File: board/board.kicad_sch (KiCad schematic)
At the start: 5 parts, among them J1 001_I2C, J2 001_I2C

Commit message: added LCSC part numbers
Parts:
- C3: lcsc (none) -> C15849

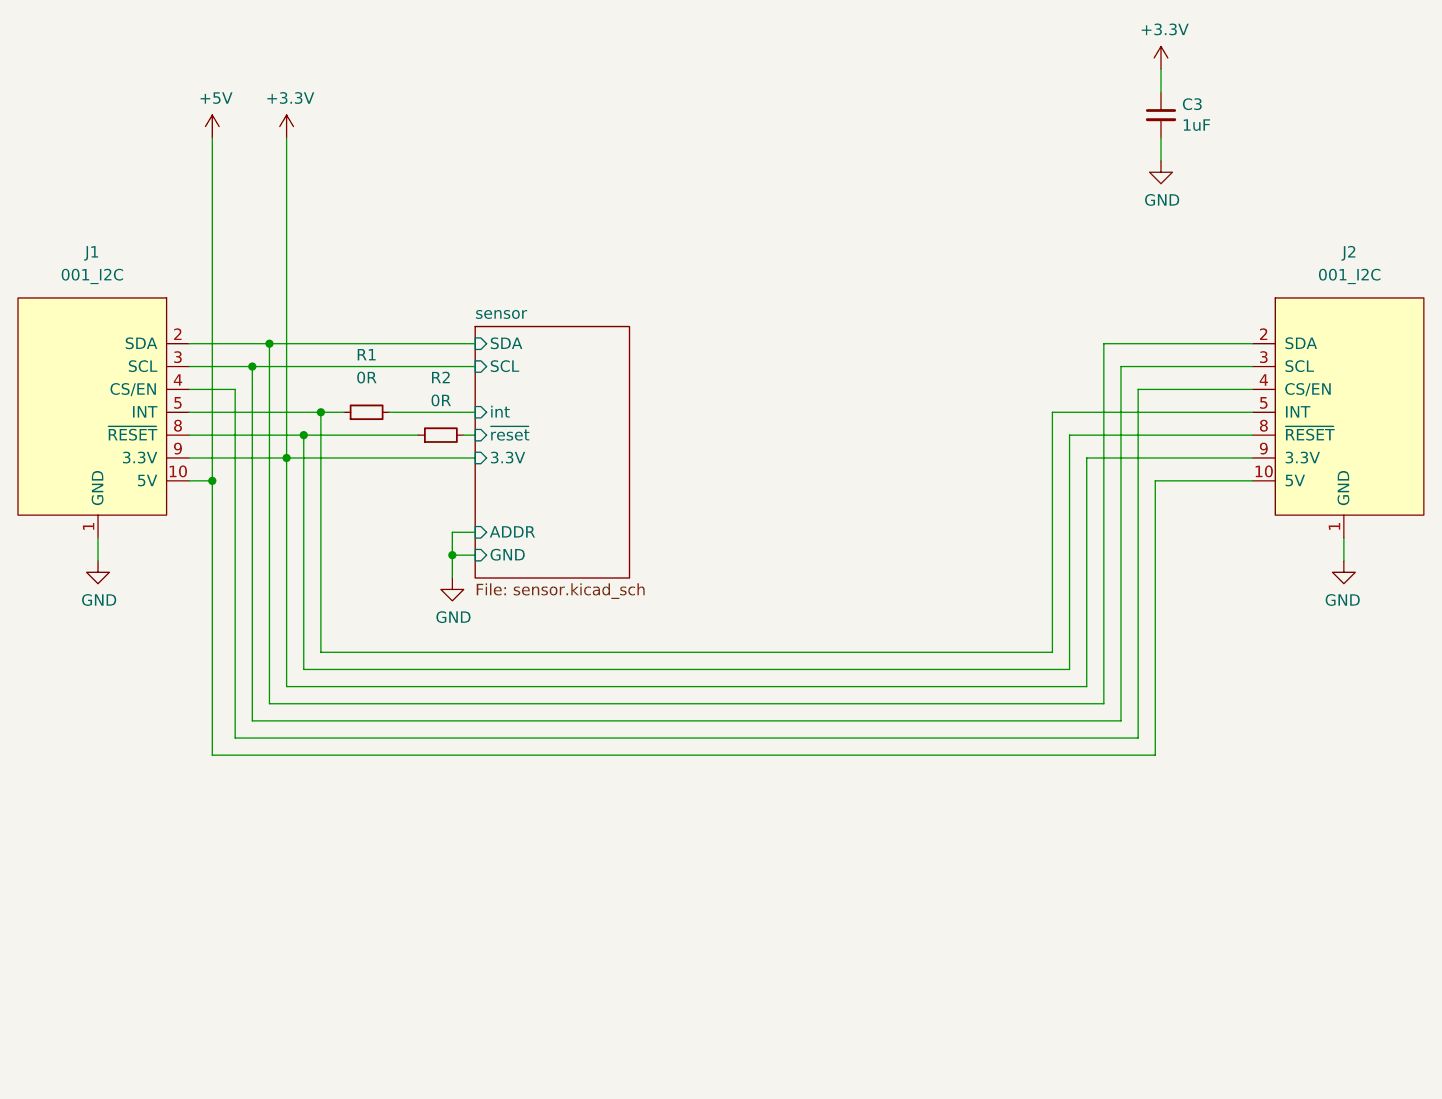
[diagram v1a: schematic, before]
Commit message: updated I2C connector to current standard
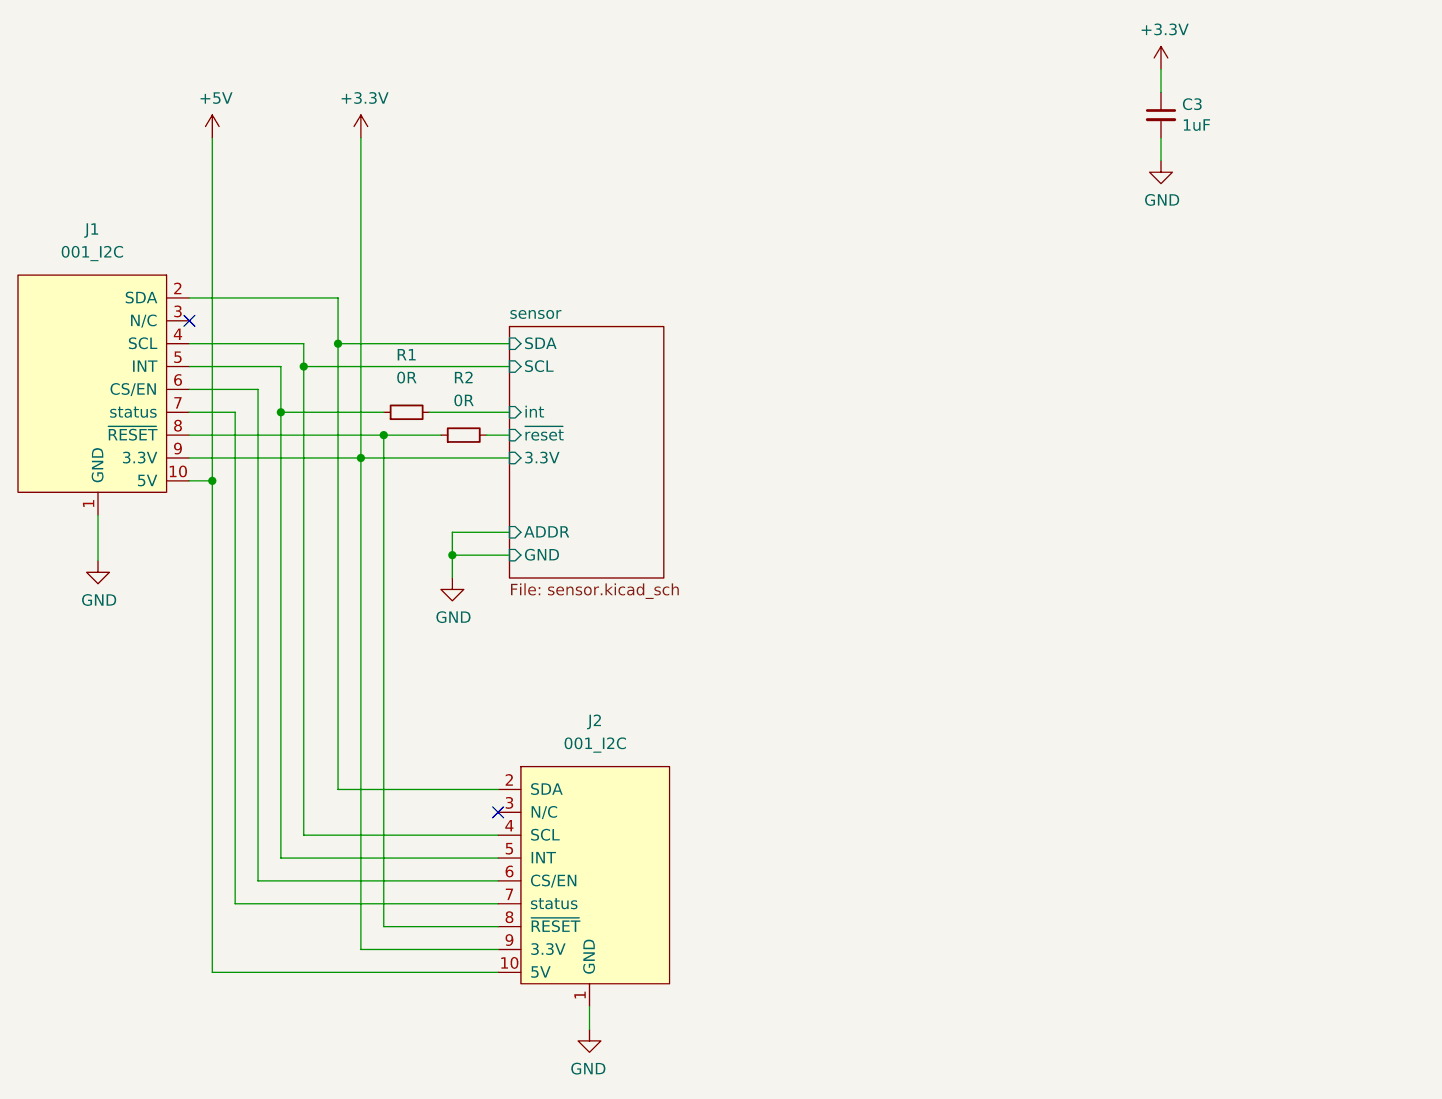
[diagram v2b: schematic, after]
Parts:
- R1, R2: lcsc (none) -> C21189
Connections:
- net sensor/SCL: now also J1.4 (SCL), J2.4 (SCL); no longer J1.3 (SCL), J2.3 (SCL)
- new net: J1.6 (CS/EN), J2.6 (CS/EN)
- new net: J1.7 (status), J2.7 (status)
- no-connect marks 0 -> 2
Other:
- moved on the sheet: R1, R2
